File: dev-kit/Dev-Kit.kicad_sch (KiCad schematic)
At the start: 0 parts

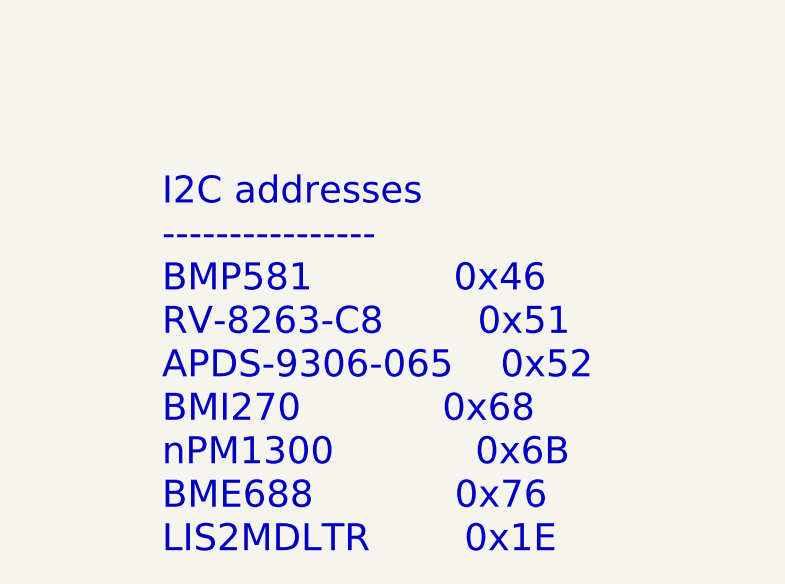
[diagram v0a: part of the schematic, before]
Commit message: PCB: Add new vibration motor
- Remove old hardware project (comes back later)
- Add new dev-kit project

Closes #102

Signed-off-by: Daniel Kampert <danielkampert@kampis-elektroecke.de>
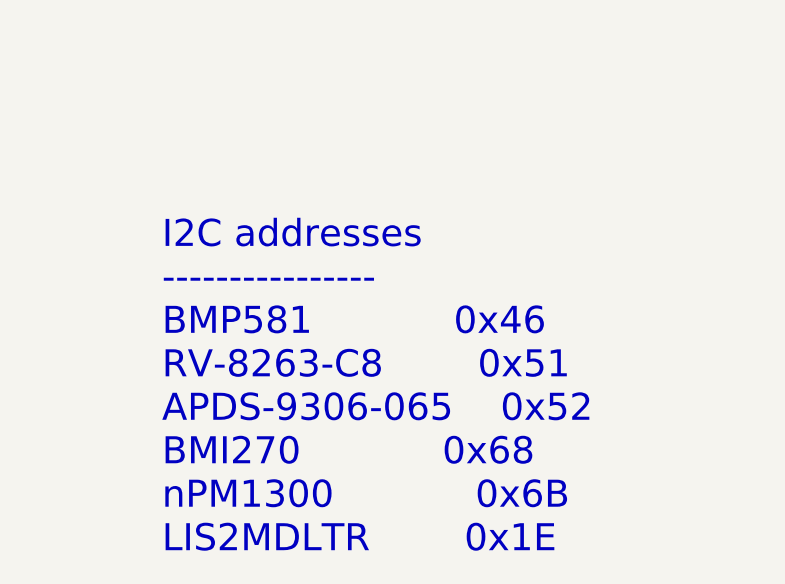
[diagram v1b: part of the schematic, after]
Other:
- note added: "I2C addresses ---------------- BMP581 0x46 RV-8263-C8 0x51 APDS-9306-065 0x52 BMI270 0x68 nPM1300 0x6B LIS2MDLTR 0x1E"
- note removed: "I2C addresses ---------------- BMP581 0x46 RV-8263-C8 0x51 APDS-9306-065 0x52 BMI270 0x68 nPM1300 0x6B BME688 0x76 LIS2MDLTR 0x1E"
- title: ZSWatch v3 -> ZSWatch v3 Dev-Kit
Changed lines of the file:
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@@
 	(paper "A4")
 	(title_block
-		(title "ZSWatch v3")
-		(date "2025-05-05")
+		(title "ZSWatch v3 Dev-Kit")
+		(date "2025-05-09")
 		(rev "0")
 		(company "github.com/jakkra/ZSWatch-HW")
 	)
-	(text "I2C addresses\n----------------\nBMP581			0x46\nRV-8263-C8		0x51\nAPDS-9306-065	0x52\nBMI270			0x68\nnPM1300			0x6B\nBME688			0x76\nLIS2MDLTR		0x1E"
+	(text "I2C addresses\n----------------\nBMP581			0x46\nRV-8263-C8		0x51\nAPDS-9306-065	0x52\nBMI270			0x68\nnPM1300			0x6B\nLIS2MDLTR		0x1E"
 		(exclude_from_sim no)
 		(at 222.25 162.56 0)
@@
 		)
 		(instances
-			(project "ZSWatch"
+			(project "Dev-Kit"
 				(path "/d5742f03-3b1a-42e5-a384-018bd4b919aa"
 					(page "3")
@@
 		)
 		(instances
-			(project "ZSWatch"
+			(project "Dev-Kit"
 				(path "/d5742f03-3b1a-42e5-a384-018bd4b919aa"
 					(page "4")
@@
 		)
 		(instances
-			(project "ZSWatch"
+			(project "Dev-Kit"
 				(path "/d5742f03-3b1a-42e5-a384-018bd4b919aa"
 					(page "2")

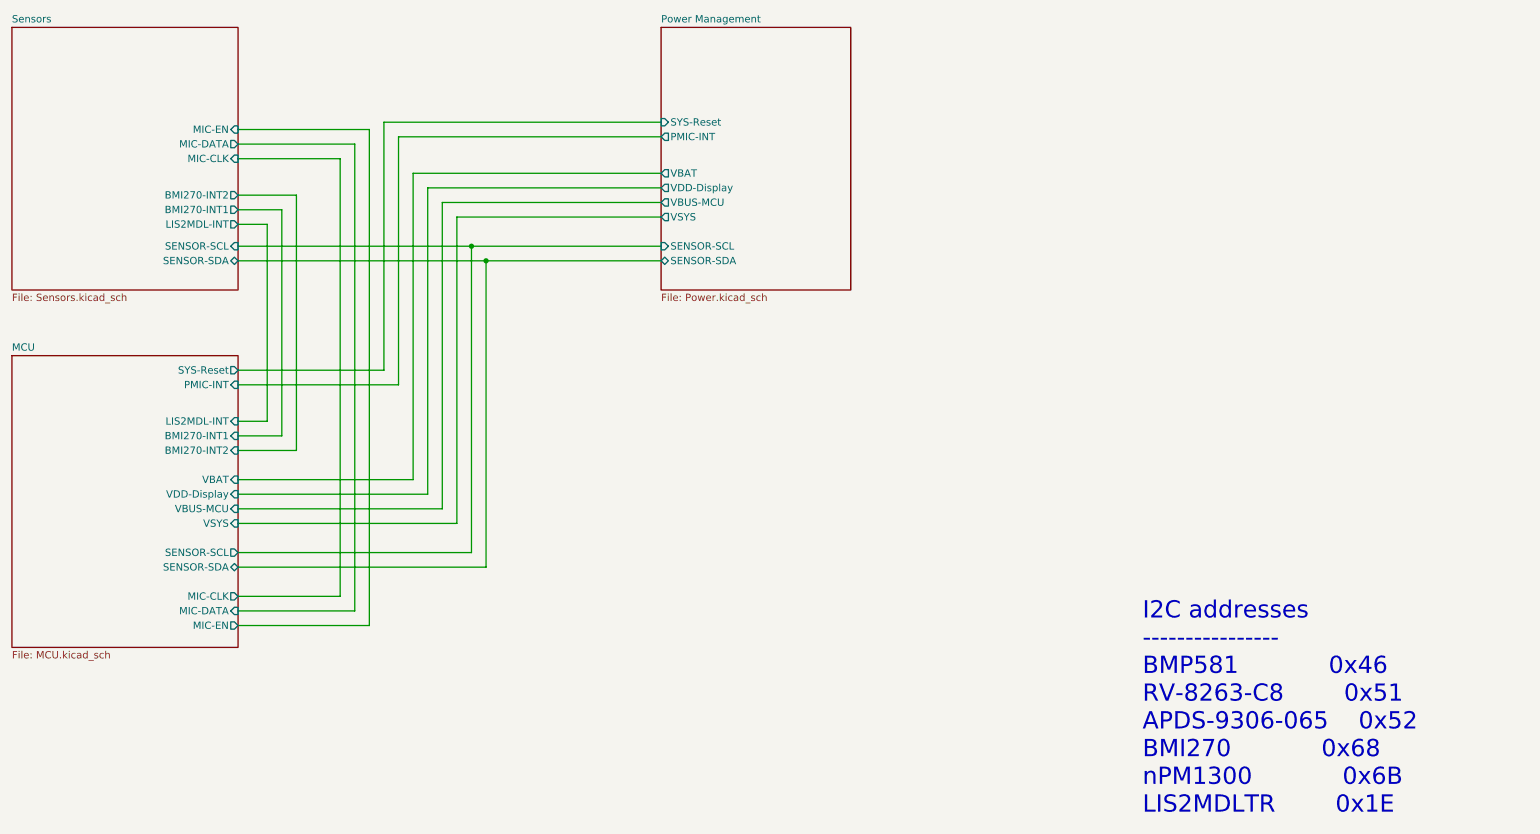
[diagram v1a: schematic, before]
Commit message: Add 0805 resistors for current measurement, reorganize schematics
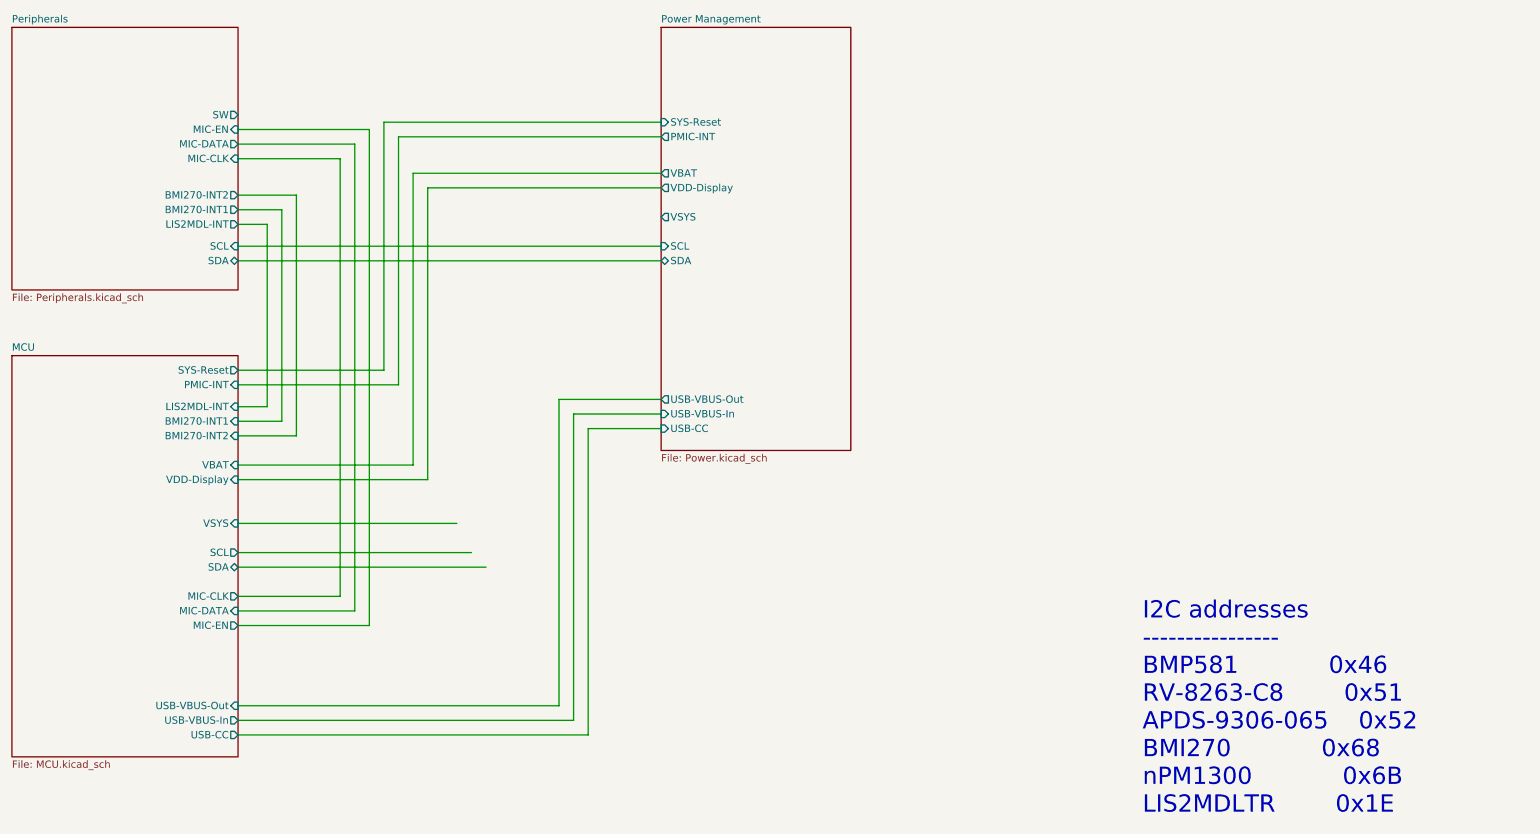
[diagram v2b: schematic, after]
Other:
- sheet Sensors renamed Peripherals
- sheet MCU ports: added SCL, SDA, USB-CC, USB-VBUS-In, USB-VBUS-Out; removed SENSOR-SCL, SENSOR-SDA, VBUS-MCU
- sheet Peripherals: file Sensors.kicad_sch -> Peripherals.kicad_sch
- sheet Peripherals ports: added SCL, SDA, SW; removed SENSOR-SCL, SENSOR-SDA
- sheet Power Management ports: added SCL, SDA, USB-CC, USB-VBUS-In, USB-VBUS-Out; removed SENSOR-SCL, SENSOR-SDA, VBUS-MCU

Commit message: Working on the layout for the dev kit
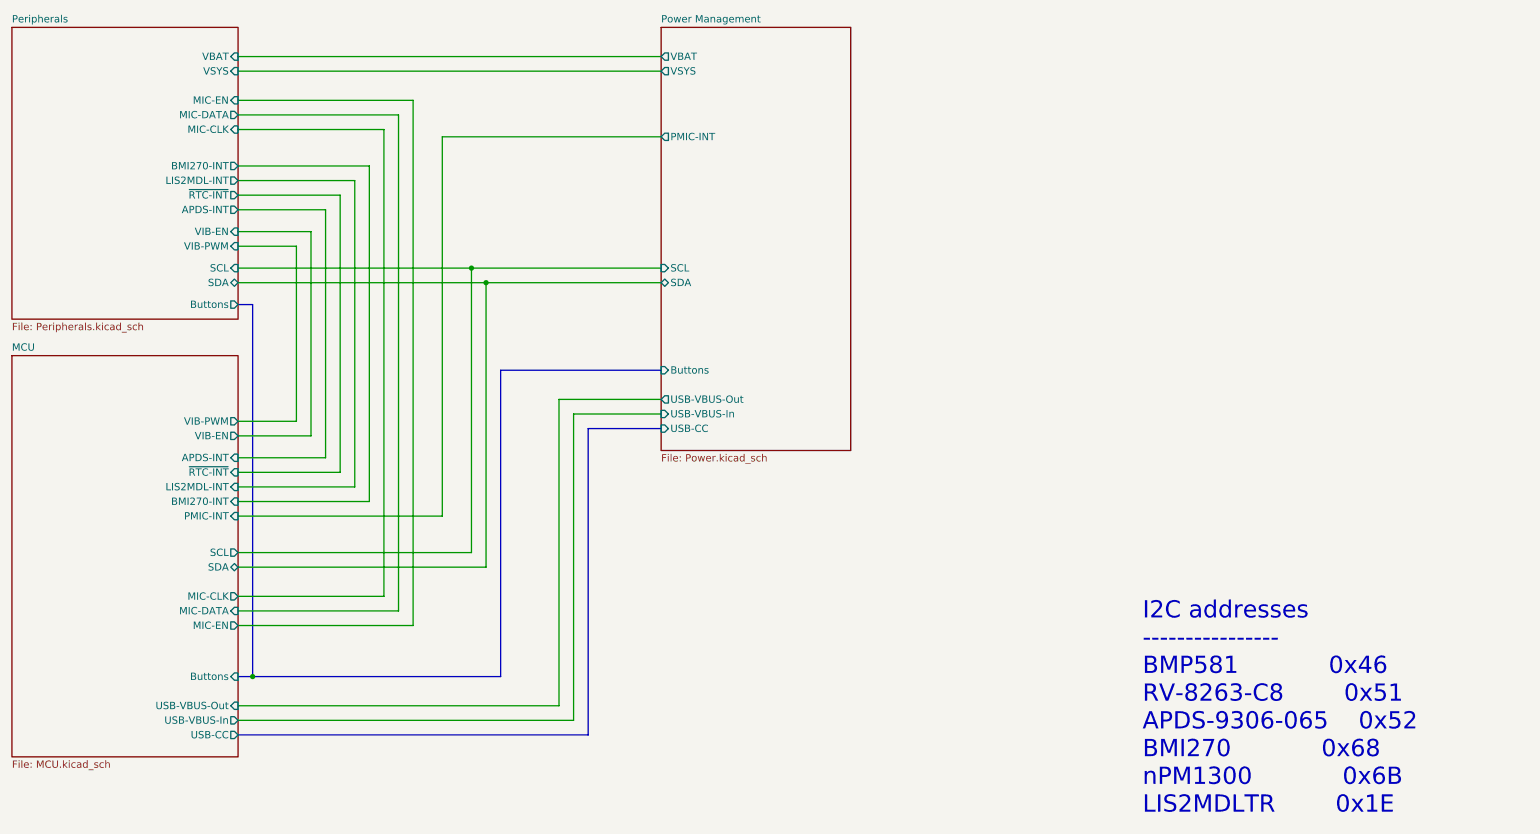
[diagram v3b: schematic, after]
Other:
- sheet MCU ports: added APDS-INT, BMI270-INT, Buttons, VIB-EN, VIB-PWM, ~{RTC-INT}; removed BMI270-INT1, BMI270-INT2, SYS-Reset, VBAT, VDD-Display, VSYS
- sheet Peripherals ports: added APDS-INT, BMI270-INT, Buttons, VBAT, VIB-EN, VIB-PWM, VSYS, ~{RTC-INT}; removed BMI270-INT1, BMI270-INT2, SW
- sheet Power Management ports: added Buttons; removed SYS-Reset, VDD-Display

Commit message: Add CI/CD pipeline for Dev-Kit, more Dev-Kit improvements
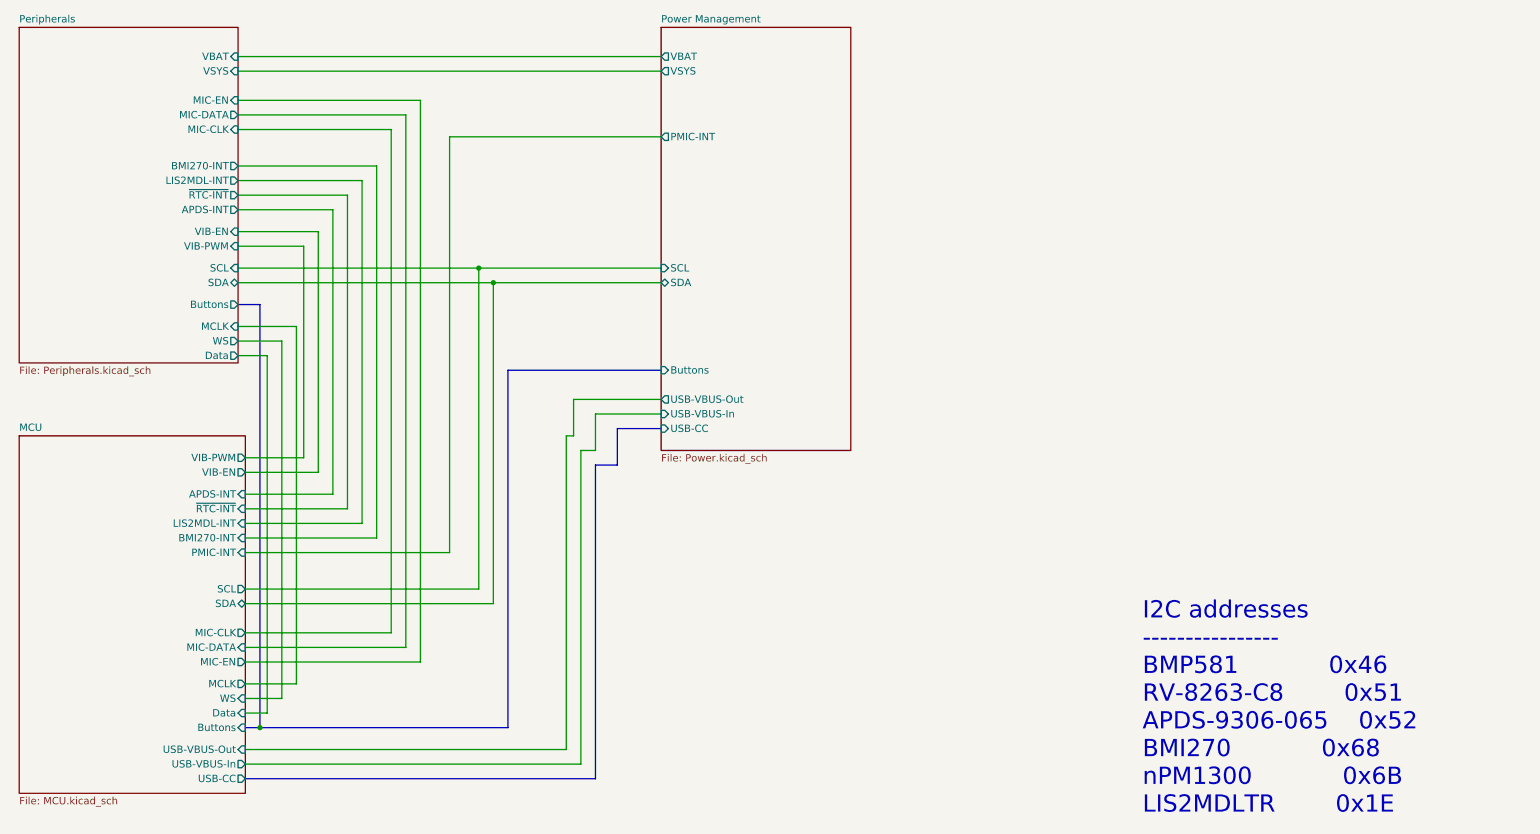
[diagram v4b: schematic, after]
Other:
- sheet MCU ports: added Data, MCLK, WS; removed none
- sheet Peripherals ports: added Data, MCLK, WS; removed none

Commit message: Changes from Jacob
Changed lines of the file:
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@@
 	(bus
 		(pts
-			(xy 130.81 95.25) (xy 138.43 95.25)
+			(xy 127 95.25) (xy 138.43 95.25)
 		)
 		(stroke
@@
 		)
 	)
-	(wire
-		(pts
-			(xy 123.19 96.52) (xy 121.92 96.52)
-		)
-		(stroke
-			(width 0)
-			(type default)
-		)
-	)
-	(wire
-		(pts
-			(xy 123.19 96.52) (xy 123.19 90.17)
-		)
-		(stroke
-			(width 0)
-			(type default)
-		)
-	)
 	(bus
 		(pts
@@
 		)
 	)
-	(bus
-		(pts
-			(xy 130.81 101.6) (xy 130.81 95.25)
-		)
-		(stroke
-			(width 0)
-			(type default)
-		)
-	)
 	(wire
 		(pts
@@
 	(wire
 		(pts
-			(xy 121.92 96.52) (xy 121.92 151.13)
+			(xy 121.92 90.17) (xy 121.92 151.13)
 		)
 		(stroke
@@
 	(wire
 		(pts
-			(xy 127 92.71) (xy 138.43 92.71)
-		)
-		(stroke
-			(width 0)
-			(type default)
-		)
-	)
-	(bus
-		(pts
-			(xy 130.81 101.6) (xy 127 101.6)
+			(xy 124.46 92.71) (xy 138.43 92.71)
 		)
 		(stroke
@@
 	(wire
 		(pts
-			(xy 124.46 153.67) (xy 124.46 99.06)
+			(xy 124.46 92.71) (xy 124.46 153.67)
 		)
 		(stroke
@@
 	(bus
 		(pts
-			(xy 127 101.6) (xy 127 156.21)
+			(xy 127 95.25) (xy 127 156.21)
 		)
 		(stroke
@@
 	(wire
 		(pts
-			(xy 123.19 90.17) (xy 138.43 90.17)
+			(xy 121.92 90.17) (xy 138.43 90.17)
 		)
 		(stroke
@@
 	(wire
 		(pts
-			(xy 127 99.06) (xy 127 92.71)
-		)
-		(stroke
-			(width 0)
-			(type default)
-		)
-	)
-	(wire
-		(pts
 			(xy 64.77 38.1) (xy 96.52 38.1)
 		)
@@
 		)
 		(stroke
-			(width 0)
-			(type default)
-		)
-	)
-	(wire
-		(pts
-			(xy 124.46 99.06) (xy 127 99.06)
-		)
-		(stroke

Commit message: Add impedance matching for USB, add jumper caps
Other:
- title: ZSWatch v3 Dev-Kit -> https://github.com/ZSWatch/Watch-HW
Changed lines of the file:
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@@
 	(paper "A4")
 	(title_block
-		(title "ZSWatch v3 Dev-Kit")
+		(title "https://github.com/ZSWatch/Watch-HW")
 		(date "2025-05-09")
 		(rev "0")
